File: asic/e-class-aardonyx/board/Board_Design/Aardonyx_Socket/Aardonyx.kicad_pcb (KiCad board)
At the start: 4 copper layers, 329 parts, among them J1 Conn_1x4, J10 Conn_1x3_M, J11 Conn_1x8, J12 Conn_1x3_M, J13 USB_B_6PIN, J14 Conn_1x4, J15 Conn_1x3_M, J16 USB_OTG, J17 Conn_1x8, J18 Conn_1x3_M, J19 Conn_1x3_M, J2 Conn_1x6, J3 Conn_1x10_F, J4 Conn_1x8_F, J5 Conn_1x8_F, J6 Conn_1x6_F, J7 Conn_1x3_M, J8 PJ-202H PWRJACK, J9 Conn_1x6, Q1 FDN339AN, SW1 FSM2JSMAATR, SW2 SW_DIP_x03, SW3 SW_SPST, U1 LSF0108PWR, U10 ADM1186, U11 FT2232H, U12 TPS7A7002DDAR, U13 TPS54627DDAR, U14 93LC56BT-I_OT, U15 TPS7A7002DDAR, U2 SKT32E, U3 IS42S32160F-TSOP2, U4 LSF0108PWR, U5 CDCE913PW, U6 ADC128S102CIMTX/NOPB, U7 74AUP1G09GW, U8 IS25LP256x-xM, U9 CAT24M01WI-GT3, Y1 27MHz, Y2 12MHz

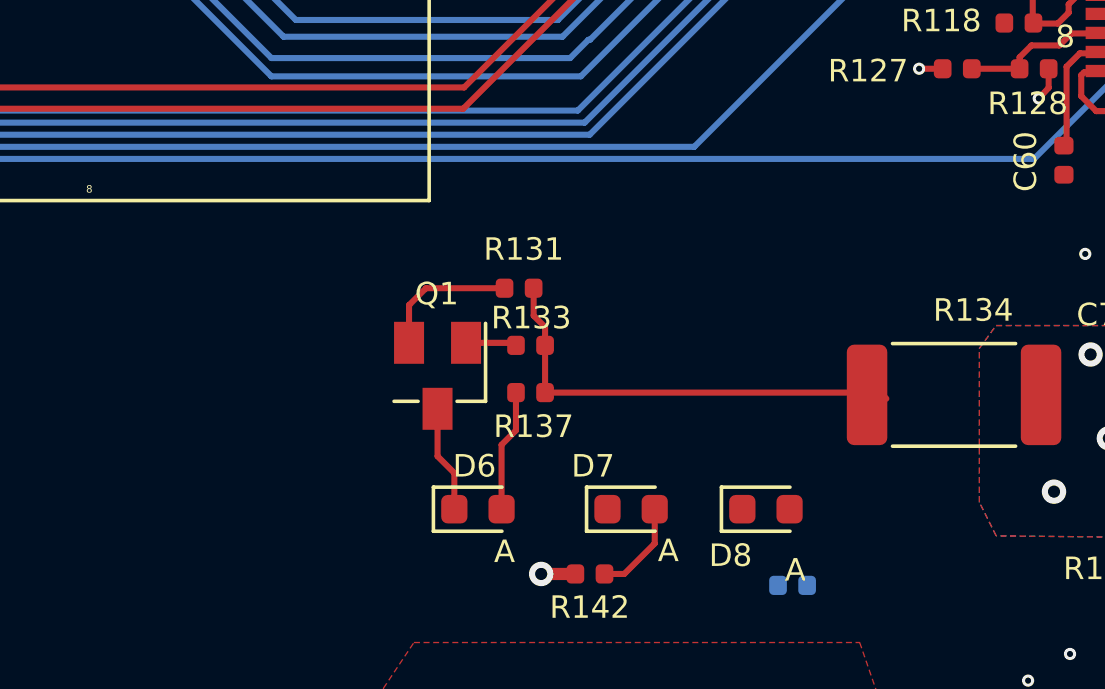
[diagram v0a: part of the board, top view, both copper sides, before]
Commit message: Updating power layer
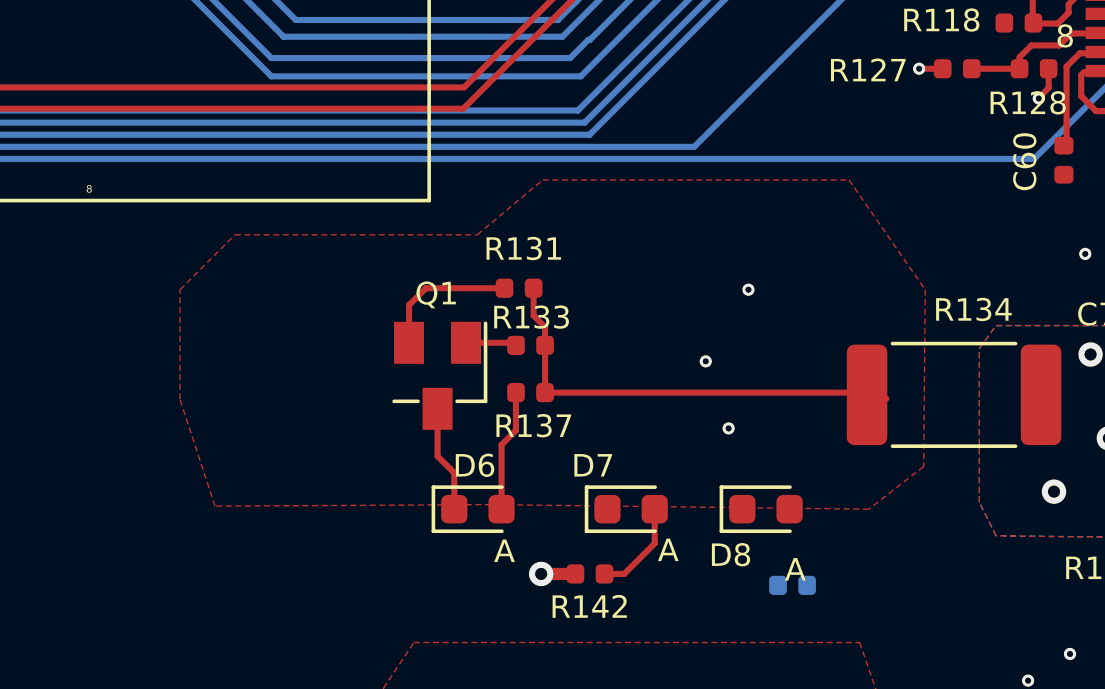
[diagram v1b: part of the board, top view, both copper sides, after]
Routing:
- net V1P8: vias 0 -> 3
- added copper zone on F.Cu, net V1P8
- added copper zone on In2.Cu, net V1P8
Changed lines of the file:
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@@
     (thickness 1.6)
     (drawings 155)
-    (tracks 4719)
+    (tracks 4722)
     (zones 0)
     (modules 329)
@@
     (0 F.Cu signal)
     (1 In1.Cu power hide)
-    (2 In2.Cu signal)
+    (2 In2.Cu signal hide)
     (31 B.Cu signal)
     (32 B.Adhes user)
@@
   (segment (start 202.4546 136.3218) (end 202.5308 136.398) (width 0.2032) (layer F.Cu) (net 160))
   (segment (start 191.7978 136.3218) (end 202.4546 136.3218) (width 0.2032) (layer F.Cu) (net 160))
+  (via (at 197.1548 135.2804) (size 0.4064) (drill 0.2032) (layers F.Cu B.Cu) (net 160))
+  (via (at 198.5772 132.8928) (size 0.4064) (drill 0.2032) (layers F.Cu B.Cu) (net 160))
+  (via (at 197.9168 137.5156) (size 0.4064) (drill 0.2032) (layers F.Cu B.Cu) (net 160))
   (segment (start 122.8492 141.1762) (end 123.6662 141.1762) (width 0.2032) (layer F.Cu) (net 161))
   (segment (start 123.6662 141.1762) (end 123.94 141.45) (width 0.2032) (layer F.Cu) (net 161))
@@
         (xy 278.638 23.9268) (xy 278.5872 88.7984) (xy 266.6492 97.6376) (xy 258.7752 97.6376) (xy 255.5748 104.4448)
         (xy 255.2192 118.5672) (xy 250.7488 121.0056) (xy 234.0356 121.0056) (xy 226.1616 127) (xy 203.0476 127)
-        (xy 179.9844 107.8484) (xy 168.5544 97.6376) (xy 168.5544 75.2348) (xy 168.1988 55.1688) (xy 164.1348 49.022)
-        (xy 161.5948 38.4048) (xy 132.2832 38.8112) (xy 114.808 38.8112) (xy 108.204 54.5084) (xy 98.1456 58.0136)
-        (xy 98.3488 94.488) (xy 110.0328 97.1804) (xy 113.4364 109.7788) (xy 125.984 109.7788) (xy 151.9936 109.2708)
-        (xy 151.892 128.778) (xy 156.5148 133.9596) (xy 165.2016 135.89) (xy 173.1772 141.732) (xy 178.5112 142.6972)
-        (xy 188.9252 142.8496) (xy 196.6468 142.6972) (xy 202.8444 145.5928) (xy 203.8096 149.606) (xy 203.6572 149.8092)
-        (xy 203.6572 154.0256) (xy 198.3232 160.5788) (xy 83.2104 160.2232) (xy 77.216 144.6276) (xy 76.8096 110.1852)
-        (xy 70.0024 106.172) (xy 44.3484 106.5784) (xy 44.1452 26.2636) (xy 54.2544 18.8468) (xy 54.2544 14.986)
-        (xy 200.5584 14.2748) (xy 273.304 14.2748)
+        (xy 179.9844 107.8484) (xy 168.5544 97.6376) (xy 168.5544 75.2348) (xy 168.3512 54.8132) (xy 152.654 52.578)
+        (xy 150.7744 41.6052) (xy 132.4864 41.5036) (xy 114.808 41.8084) (xy 113.03 54.5084) (xy 100.838 58.0644)
+        (xy 100.6348 93.726) (xy 110.0328 97.1804) (xy 113.4364 109.7788) (xy 125.984 109.7788) (xy 145.847092 109.857465)
+        (xy 145.8976 125.1712) (xy 150.7236 135.3312) (xy 156.8196 135.6868) (xy 162.2552 135.7884) (xy 173.228 142.8496)
+        (xy 178.562 142.8496) (xy 188.9252 142.8496) (xy 196.6468 142.8496) (xy 200.66 145.3388) (xy 203.7588 147.6756)
+        (xy 203.6572 149.8092) (xy 203.6572 154.0256) (xy 198.3232 160.5788) (xy 83.3628 160.6296) (xy 77.216 144.6276)
+        (xy 76.8096 110.1852) (xy 70.0024 106.172) (xy 44.3484 106.5784) (xy 44.1452 26.2636) (xy 54.2544 18.8468)
+        (xy 54.2544 14.986) (xy 200.8632 15.24) (xy 273.4564 15.1384)
+      )
+    )
+  )
+  (zone (net 160) (net_name V1P8) (layer In2.Cu) (hatch edge 0.508)
+    (connect_pads yes (clearance 0.508))
+    (min_thickness 0.254)
+    (fill yes (arc_segments 32) (thermal_gap 0.508) (thermal_bridge_width 0.762))
+    (polygon
+      (pts
+        (xy 153.416 58.0644) (xy 155.2956 60.2488) (xy 155.194 87.3252) (xy 159.8676 87.376) (xy 166.7256 87.0712)
+        (xy 166.7256 99.5172) (xy 191.4652 122.2756) (xy 191.262 129.032) (xy 197.8152 128.8288) (xy 204.5716 132.8928)
+        (xy 204.3684 132.9436) (xy 204.3684 138.8872) (xy 202.5904 140.1572) (xy 174.5996 140.1572) (xy 159.4104 129.54)
+        (xy 150.114 123.9012) (xy 150.4188 110.0328) (xy 150.3172 96.9772) (xy 116.2304 97.3328) (xy 112.6744 93.8784)
+        (xy 112.4712 60.452) (xy 115.7732 55.8292) (xy 151.384 55.9816)
+      )
+    )
+  )
+  (zone (net 160) (net_name V1P8) (layer F.Cu) (hatch edge 0.508)
+    (connect_pads yes (clearance 0.508))
+    (min_thickness 0.254)
+    (fill yes (arc_segments 32) (thermal_gap 0.508) (thermal_bridge_width 0.762))
+    (polygon
+      (pts
+        (xy 204.47 132.8928) (xy 204.4192 138.7856) (xy 202.5904 140.208) (xy 189.992 140.0556) (xy 180.7972 140.1064)
+        (xy 179.6288 136.5504) (xy 179.6288 132.8928) (xy 181.4576 131.064) (xy 189.5348 131.064) (xy 191.7192 129.2352)
+        (xy 201.93 129.2352)
       )
     )

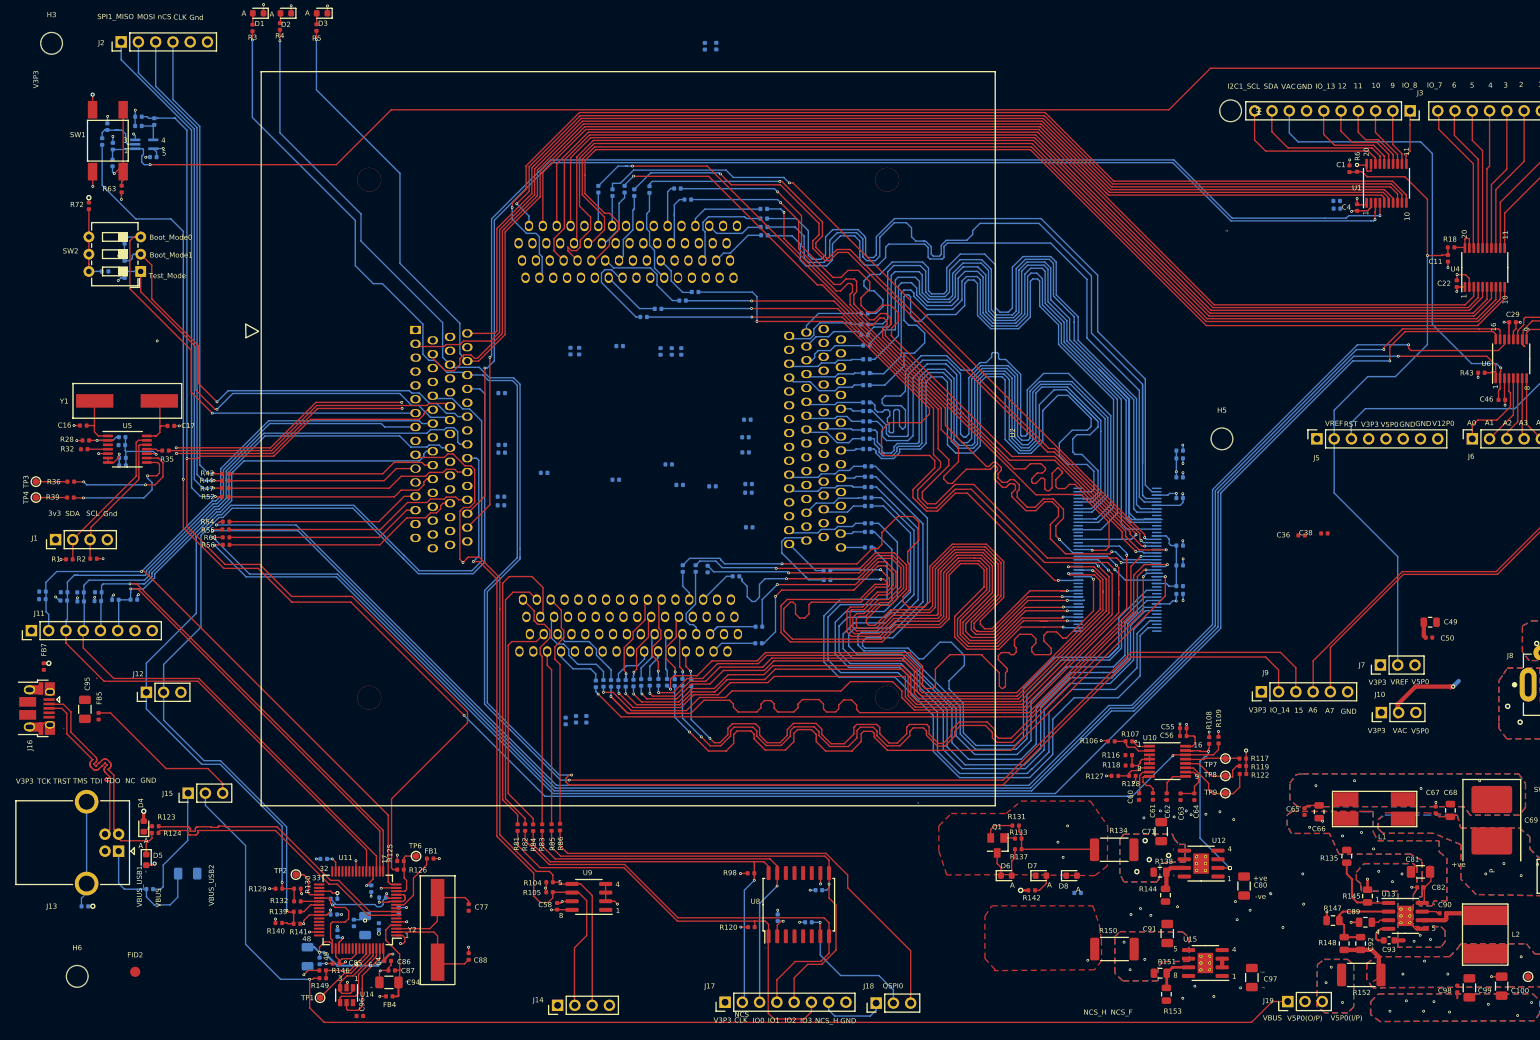
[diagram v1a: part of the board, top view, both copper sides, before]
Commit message: updated soc track
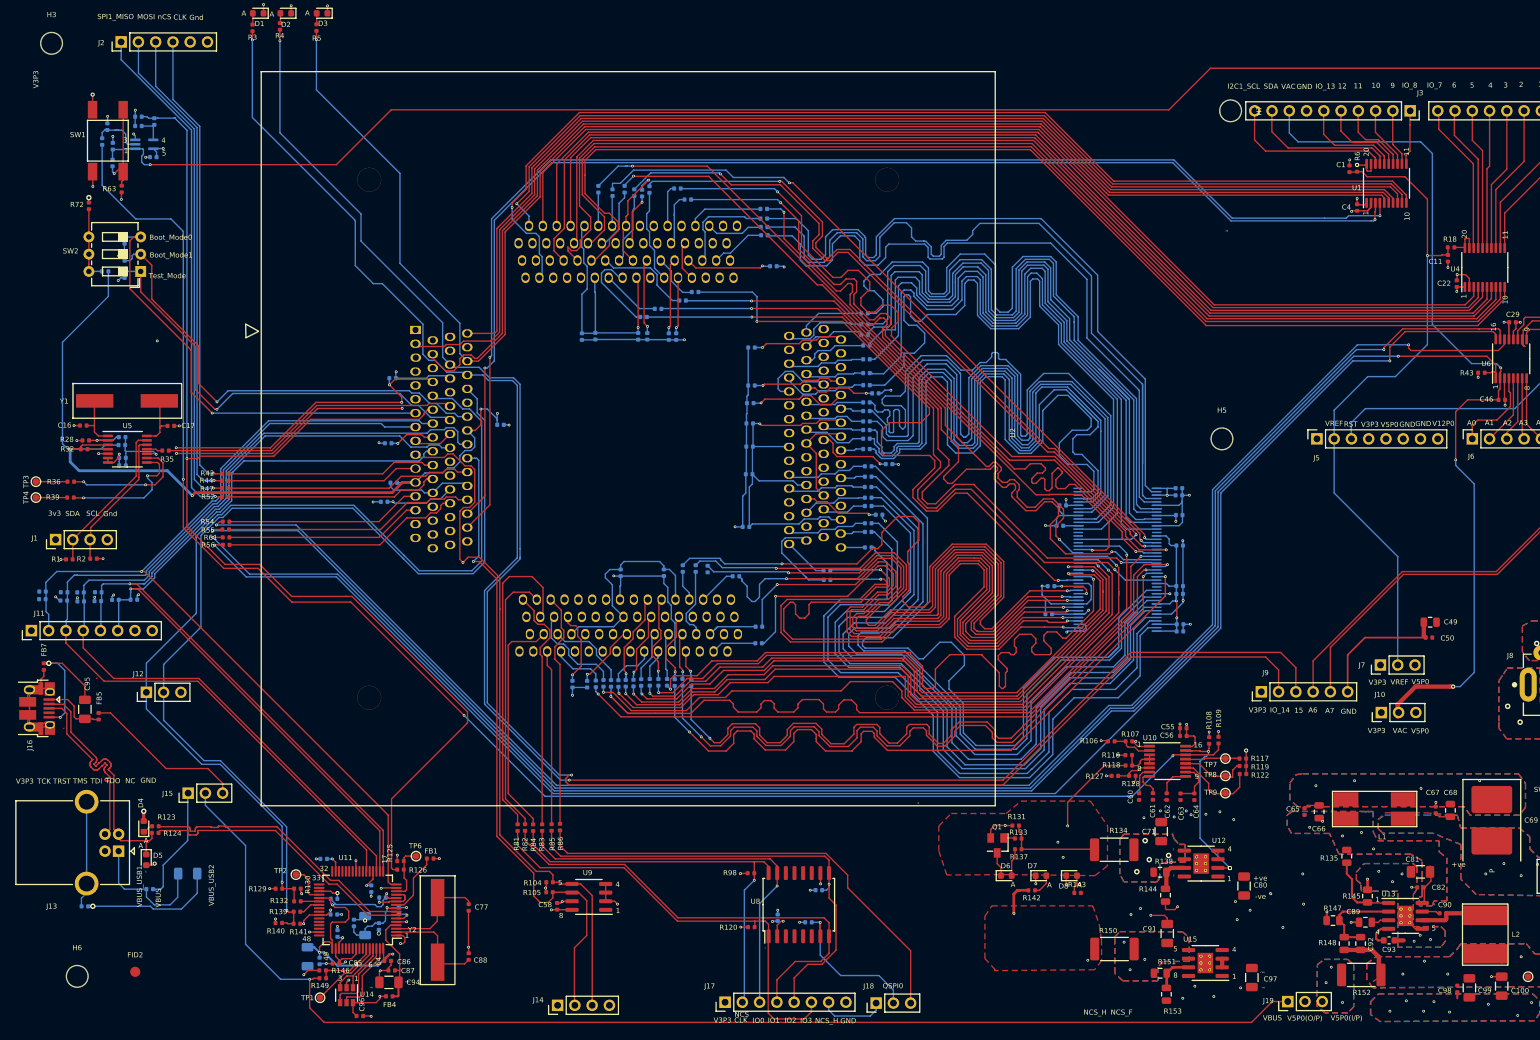
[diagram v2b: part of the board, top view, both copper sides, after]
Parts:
- C36, C38: moved to B.Cu
- R143: moved to F.Cu
- moved C15 73.2 mm to (195.8, 101.7)
- moved C21 70.6 mm to (196.1, 97.6)
- moved C2 46.4 mm to (127.1, 60.9), turned to 270 degrees
- moved C3 46.2 mm to (129.1, 60.8), turned to 270 degrees
- moved C36 35.6 mm to (197.4, 88.7)
- moved C39 29.7 mm to (170.8, 87.1), turned to 0 degrees
- moved C13 26.5 mm to (152.1, 62.5), turned to 180 degrees
- moved C54 22.9 mm to (139.2, 95.6), turned to 90 degrees
- moved C25 22.9 mm to (170.3, 69.2)
- moved C7 22.7 mm to (136.0, 39.8), turned to 90 degrees
- moved C18 22.7 mm to (215.1, 104.3)
- moved C52 22.5 mm to (132.8, 95.7)
- moved C38 22.4 mm to (214.9, 83.2), turned to 0 degrees
- moved C33 21.5 mm to (172.3, 79.7)
- moved C48 20.4 mm to (151.3, 88.9)
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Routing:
- net V1P8: track 15.1 -> 349.5 mm, vias 3 -> 16
- net GND: track 221.8 -> 514.5 mm, vias 114 -> 134
- net V3P3: track 110.6 -> 256.6 mm, vias 44 -> 59
- net VAC: track 81.1 -> 129.8 mm, vias 2 -> 3
- net /sdram/SDRAM_D5: track 129.9 -> 107.5 mm
- net Net-(FB7-Pad2): track 2.54 -> 19.1 mm
- net Net-(C78-Pad1): track 0.00 -> 10.6 mm, vias 0 -> 1
- net Net-(C95-Pad1): track 0.00 -> 9.45 mm
- net Net-(R136-Pad1): track 0.00 -> 3.03 mm, vias 0 -> 1
- net Net-(D8-Pad2): track 0.00 -> 2.70 mm
- net Net-(U11-Pad63): track 13.8 -> 11.8 mm
- net /sdram/SDRAM_D8: track 100.6 -> 99.0 mm
- net V5P0: track 1.95 -> 3.22 mm
- net /ftdi/UART0_TX: track 147.0 -> 145.9 mm
- net Net-(U11-Pad61): track 12.0 -> 10.9 mm
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
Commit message: Updated layout
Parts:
- R3, R4, R5, R98: moved to B.Cu
- moved C49 22.4 mm to (252.3, 80.5)
- moved C50 22.4 mm to (252.1, 82.8)
- moved J7 19.2 mm to (244.9, 90.0)
- moved J10 16.7 mm to (244.9, 99.5)
- moved J9 13.5 mm to (224.9, 99.9)
- moved C74 9.53 mm to (62.9, 147.1), turned to 270 degrees
- moved C17 7.90 mm to (64.2, 66.5), turned to 180 degrees
- moved C16 7.81 mm to (56.1, 66.5), turned to 0 degrees
- moved J12 6.75 mm to (67.7, 118.1)
- moved R98 4.59 mm to (155.9, 142.3), turned to 0 degrees
- moved R121 4.52 mm to (160.5, 151.6)
- moved C27 4.22 mm to (55.3, 78.8), turned to 90 degrees
- moved D1 4.14 mm to (79.0, 17.4)
- moved D3 4.14 mm to (88.4, 17.4)
- moved D2 4.12 mm to (83.7, 17.4)
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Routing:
- net V5P0: track 3.22 -> 111.9 mm, vias 4 -> 5
- net GND: track 514.5 -> 412.9 mm, vias 134 -> 161
- net V1P8: track 349.5 -> 437.6 mm, vias 16 -> 24
- net V12P0: track 6.11 -> 84.2 mm
- net /arduino_header/A7: track 95.1 -> 57.8 mm, vias 0 -> 1
- net /arduino_header/A6: track 96.2 -> 60.1 mm, vias 0 -> 1
- net VAC: track 129.8 -> 106.5 mm, vias 3 -> 1
- net VREF_AH: track 97.8 -> 83.4 mm
- net /ftdi/TCK: track 138.9 -> 153.0 mm, vias 1 -> 0
- net Net-(R68-Pad2): track 1.09 -> 14.0 mm, vias 0 -> 1
- net /RESET: track 186.5 -> 175.5 mm
- net /ftdi/USB_D+: track 29.6 -> 37.6 mm, vias 0 -> 1
- net Net-(R39-Pad2): track 19.6 -> 11.7 mm, vias 2 -> 0
- net Net-(C17-Pad1): track 8.22 -> 15.9 mm
- net /power_2/V18_EN: track 27.1 -> 34.8 mm
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- added copper zone on F.Cu, net Net-(C90-Pad2)
- added copper zone on B.Cu, net V5P0
- added copper zone on F.Cu, net V5P0
